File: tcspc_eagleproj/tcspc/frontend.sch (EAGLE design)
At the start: 63 parts, among them Q2 ALD1101SAL, U2 MCP4725, U3 ADCMP582, U4 LT6003_SOT23-5, U5 LT6003_SOT23-5, X1 SMA, X2 SMA

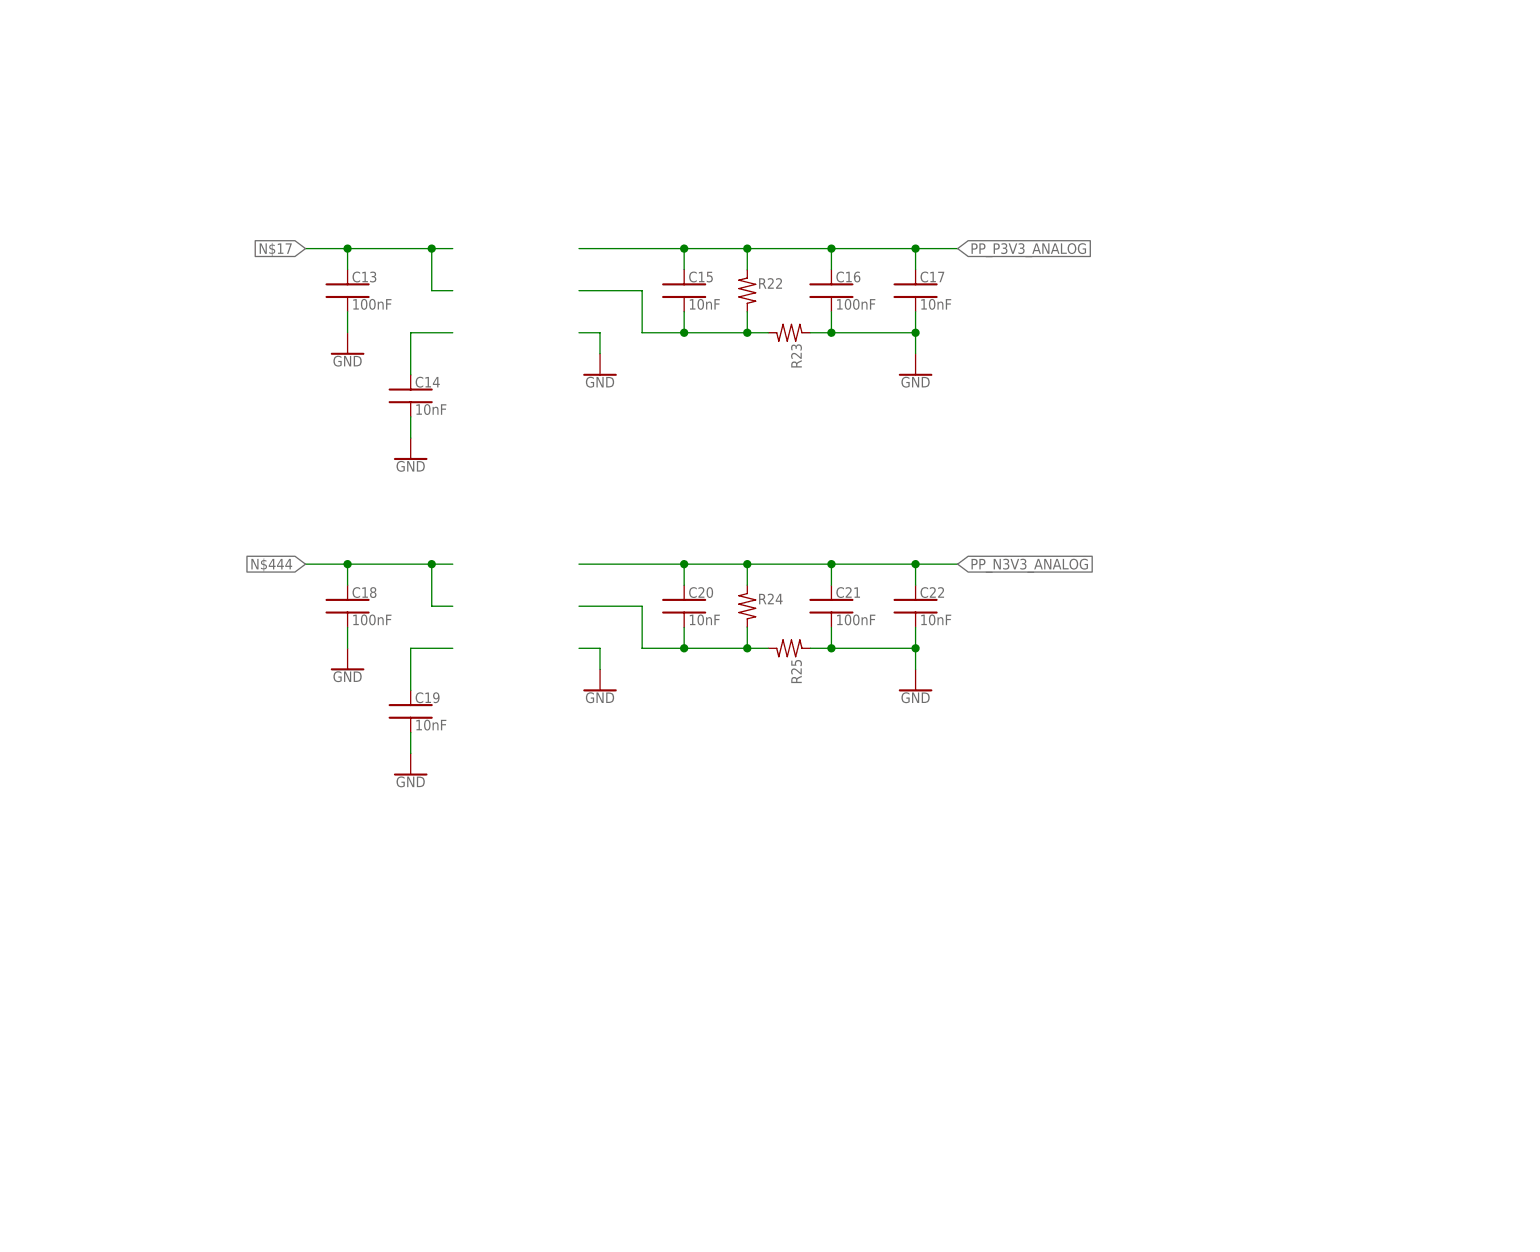
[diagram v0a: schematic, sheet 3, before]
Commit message: added the postregs to the frontend schematic, and also the output LVDS to TTL converter, only major thing left is to add testpoints places.
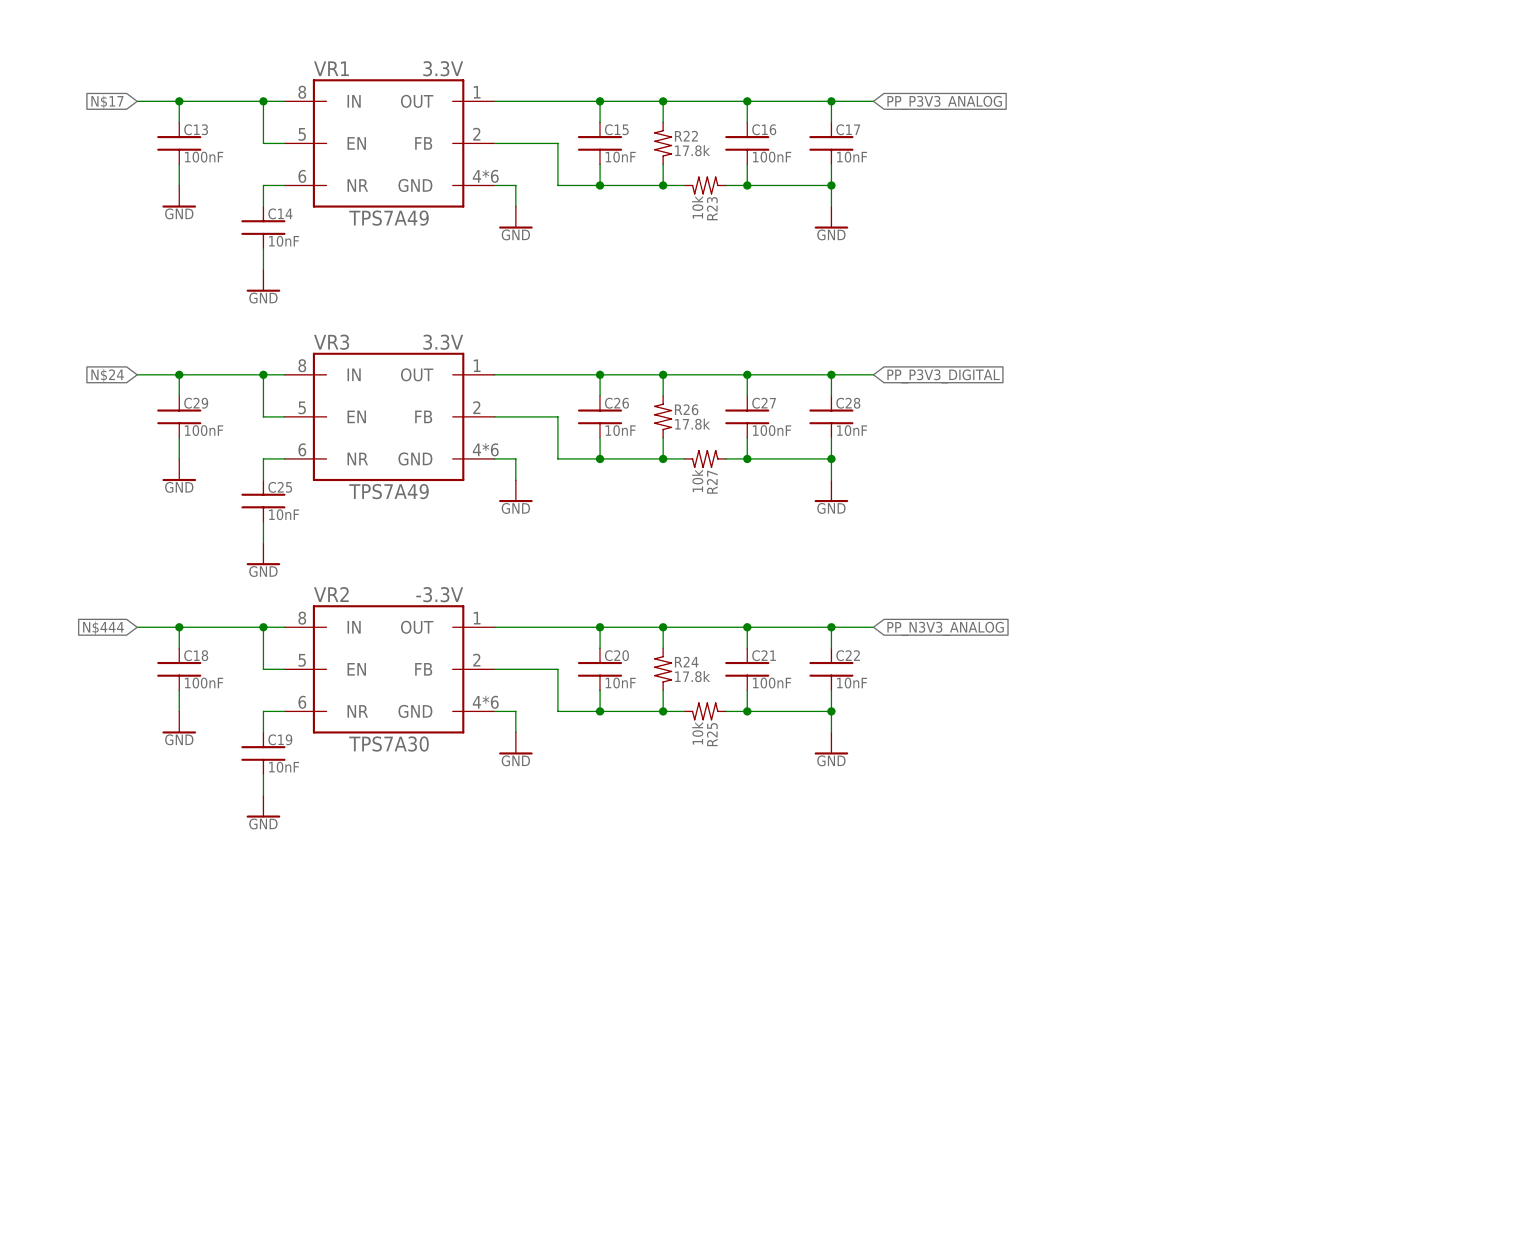
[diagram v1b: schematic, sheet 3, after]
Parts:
- added C23, C27, C29: 100nF, tcspc_lib:CAP_0402
- added C24, C25, C26, C28: 10nF, tcspc_lib:CAP_0402
- added R26: 17.8k, tcspc_lib:RES_0402
- added R27: 10k, tcspc_lib:RES_0402
- added U1: DS90LV028AQ, tcspc_lib:DS90LV028AQ
- added VR1, VR3: 3.3V, tcspc_lib:TPS7A49
- added VR2: -3.3V, tcspc_lib:TPS7A30
- C10, C11, C12, C3, C4, C53, C54, C55, C6, C7, C8, C9: value .1uF -> 100nF
- R22, R24: value (none) -> 17.8k
- R23, R25: value (none) -> 10k
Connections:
- new net N$15: U1.OUT-A, X2.1
- new net N$16: C25.1, VR3.NR
- new net N$21: C26.2, R26.2, R27.2, VR3.FB
- new net N$24: C29.1, VR3.EN, VR3.IN
- net !CHA_LVDS_OUT: now also U1.!IN-A
- net CHA_LVDS_OUT: now also U1.IN-A
- net GND: now also C23.2, C24.2, C25.2, C27.2, C28.2, C29.2, R27.1, U1.GND, VR1.GND, VR2.GND, VR3.GND, X2.GND
- net N$17: now also VR1.EN, VR1.IN
- net N$19: now also VR1.NR
- net N$25: now also VR2.NR
- net N$4: now also VR2.FB
- net N$444: now also VR2.EN, VR2.IN
- net N$5: now also VR1.FB
- net PP_N3V3_ANALOG: now also VR2.OUT
- net PP_P3V3_ANALOG: now also VR1.OUT
- net PP_P3V3_DIGITAL: now also C23.1, C24.1, C26.1, C27.1, C28.1, R26.1, U1.VCC, VR3.OUT
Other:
- moved on the sheet: C13, C14, C15, C16, C17, C18, C19, C20, C21, C22, C55, R22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

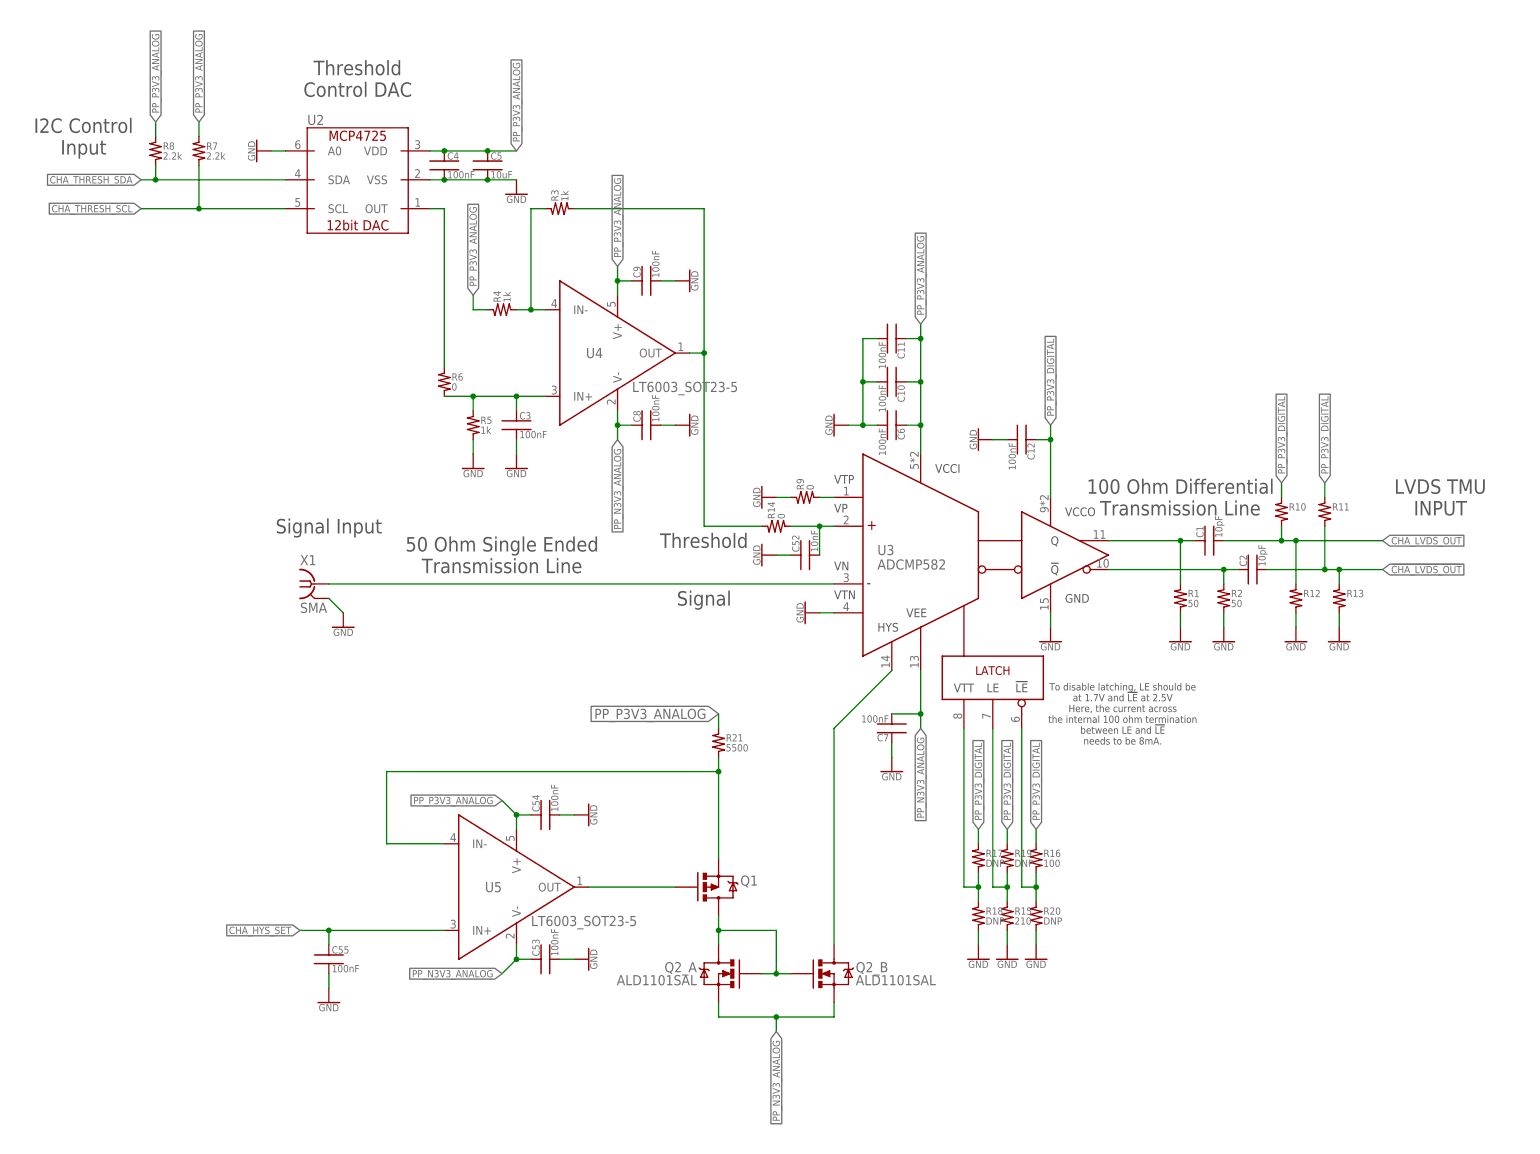
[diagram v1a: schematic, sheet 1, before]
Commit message: The frontend schematic seems done, added more testpoints and replaced the single dacs with a eight channel 12 bit dac, and added a spot to stick datasheets for the parts
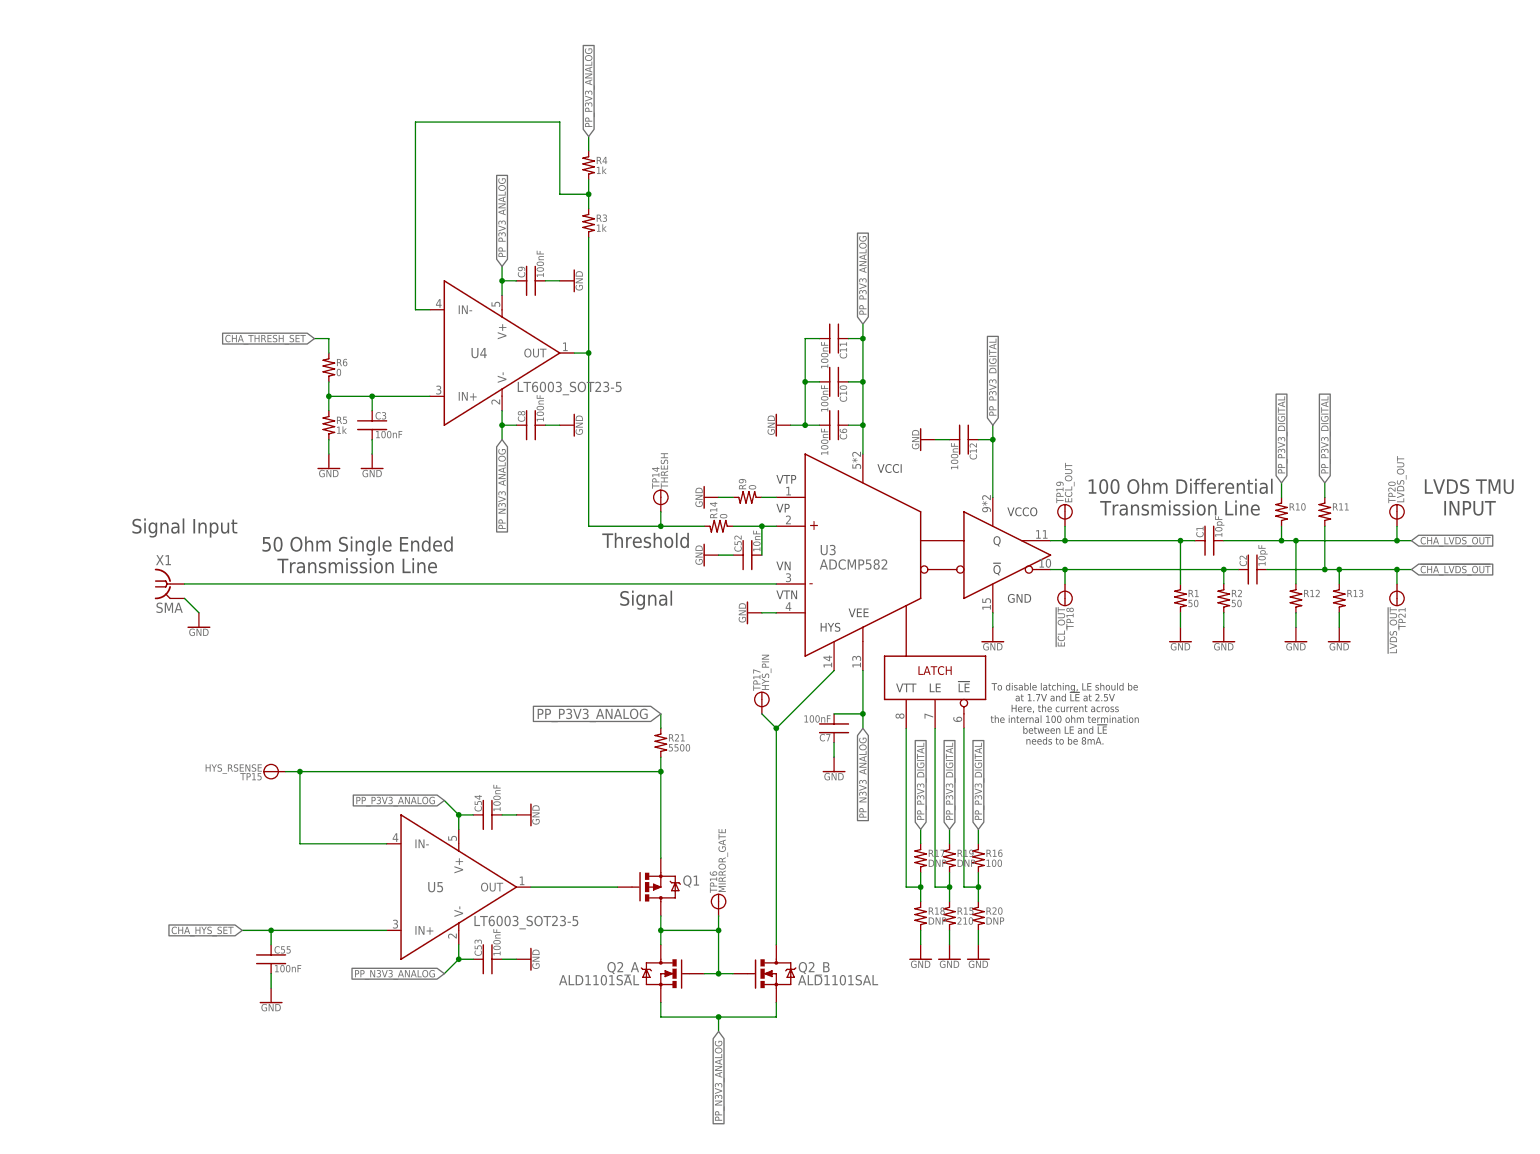
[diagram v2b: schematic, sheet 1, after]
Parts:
- removed C4: 100nF, tcspc_lib:CAP_0402
- removed C5: 10uF, tcspc_lib:CAP_0402
- removed R7, R8: 2.2k, tcspc_lib:RES_0402
- removed U2: MCP4725, tcspc_lib:MCP4725
- added C30: 100nF, tcspc_lib:CAP_0402
- added C31: 10uF, tcspc_lib:CAP_0402
- added TP10: DAC_OUT_A, tcspc_lib:TESTPOINT_A
- added TP11: DAC_OUT_B, tcspc_lib:TESTPOINT_A
- added TP12: DAC_OUT_E, tcspc_lib:TESTPOINT_A
- added TP13: DAC_OUT_H, tcspc_lib:TESTPOINT_A
- added TP14: THRESH, tcspc_lib:TESTPOINT_A
- added TP15: HYS_RSENSE, tcspc_lib:TESTPOINT_A
- added TP16: MIRROR_GATE, tcspc_lib:TESTPOINT_A
- added TP17: HYS_PIN, tcspc_lib:TESTPOINT_A
- added TP18: !ECL_OUT, tcspc_lib:TESTPOINT_A
- added TP19: ECL_OUT, tcspc_lib:TESTPOINT_A
- added TP20: LVDS_OUT, tcspc_lib:TESTPOINT_A
- added TP21: !LVDS_OUT, tcspc_lib:TESTPOINT_A
- added TP5: P3V3D, tcspc_lib:TESTPOINT_A
- added TP6: P3V3A, tcspc_lib:TESTPOINT_A
- added TP7: N3V3A, tcspc_lib:TESTPOINT_A
- added TP8, TP9: (no value), tcspc_lib:TESTPOINT_A
- added U6: AD53X8, tcspc_lib:AD53X8
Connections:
- net N$444 renamed PP_N5V_VIN
- removed net CHA_THRESH_SCL: R7.2, TP4.TP, U2.SCL
- removed net CHA_THRESH_SDA: R8.2, TP3.TP, U2.SDA
- removed net N$14: TP2.TP
- removed net N$17: C13.1, VR1.EN, VR1.IN
- removed net N$24: C29.1, VR3.EN, VR3.IN
- new net CHA_THRESH_SET: R6.1, TP10.TP, U6.VOUT_A
- new net N$20: TP9.TP
- new net PP_P5V_VIN: C13.1, C29.1, VR1.EN, VR1.IN, VR3.EN, VR3.IN
- new net T/H_DAC_!LDAC!: TP4.TP, U6.!LDAC
- new net T/H_DAC_!SYNC!: TP2.TP, U6.!SYNC
- new net T/H_DAC_DIN: TP3.TP, TP8.TP, U6.DIN
- new net T/H_DAC_SCLK: TP1.TP, U6.SCLK
- net !CHA_LVDS_OUT: now also TP21.TP
- net CHA_HYS_SET: now also TP11.TP, U6.VOUT_B
- net CHA_LVDS_OUT: now also TP20.TP
- net GND: now also C30.2, C31.2, U6.GND; no longer C4.2, C5.2, U2.A0, U2.VSS
- net N$1: now also TP15.TP
- net N$11: now also TP13.TP, U6.VOUT_H; no longer TP1.TP
- net N$13: now also TP14.TP
- net N$2: now also TP16.TP
- net N$3: now also TP18.TP
- net N$42: now also TP17.TP
- net N$6: now also TP19.TP
- net N$8: now also TP12.TP, U6.VOUT_E; no longer R6.1, U2.OUT
- net PP_N3V3_ANALOG: now also TP7.TP
- net PP_P3V3_ANALOG: now also TP6.TP, U6.VREF_ABCD, U6.VREF_EFGH; no longer C4.1, C5.1, R7.1, R8.1, U2.VDD
- net PP_P3V3_DIGITAL: now also C30.1, C31.1, TP5.TP, U6.V_DD
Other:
- note removed: "I2C Control Input"
- note removed: "Threshold Control DAC"
- moved on the sheet: C10, C11, C12, C3, C52, C53, C54, C55, C6, C7, C8, C9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
